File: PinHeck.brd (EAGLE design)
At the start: 359.2 x 152.3 mm, 338 parts, among them IC1 FT232RQ-REEL, IC2 PIC32MX795F512L-80I/PT, IC3 CD74HCT244E, IC4 CD74HCT244E, IC5 ULN2803A, J1 500075-1517, J11 No Load, J2 500075-1517, J3 N/A, J6 161-3507-E, P1 TC33X-2-103E, SW1 101-0134-EV, SW2 101-0134-EV, U1 P8X32A-Q44, U10 74HCT2G04GV,125, U11 74HC165D,652, U12 74HC165D,652, U14 MC74HC08ADG, U15 MC74HC08ADG, U16 MC74HC08ADG, U17 MC74HC08ADG, U18 MC74HC08ADG, U19 MC74HC08ADG, U2 FT230XS-R, U20 TIP107, U21 TIP107, U22 TIP107, U23 TIP107, U24 TIP107, U25 TIP107, U26 TIP107, U27 TIP107, U28 TIP102, U29 TIP102, U3 74HC595D-Q100, U30 TIP102, U31 TIP102, U32 TIP102, U33 TIP102, U34 TIP102, U35 TIP102, U36 WS2801, U37 TIP102, U38 WS2801, U39 LM2937IMP-3.3/NOPB, U4 CAT24M01XI-T2, U40 TIP102, U41 TIP102, U42 TIP102, U43 TIP102, U44 TIP102, U45 TIP102, U46 TIP102, U47 TIP102, U48 TIP102, U49 TIP102, U5 74HC595D-Q100, U50 TIP102, U51 TIP102, U52 CD74HC123M96, U6 TIP102, U7 TIP102, U8 TIP102, U9 TIP102, X1 FQ7050B-8.000, X2 ECS-65-20-4X

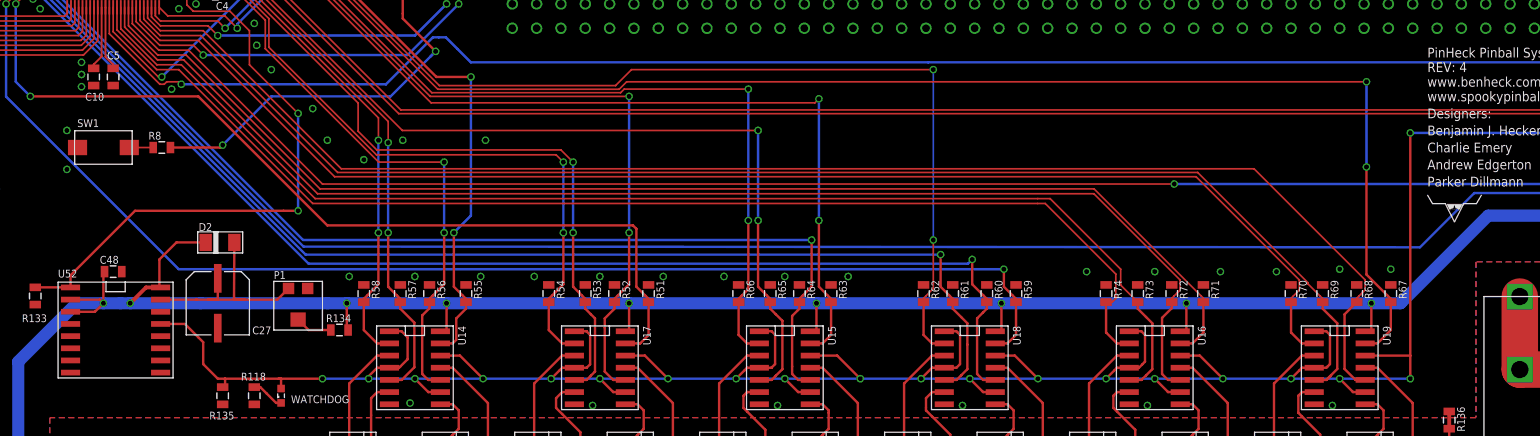
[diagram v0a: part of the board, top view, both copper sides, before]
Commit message: Rev 5 push. Fixed Bom issues and pinout for 556.
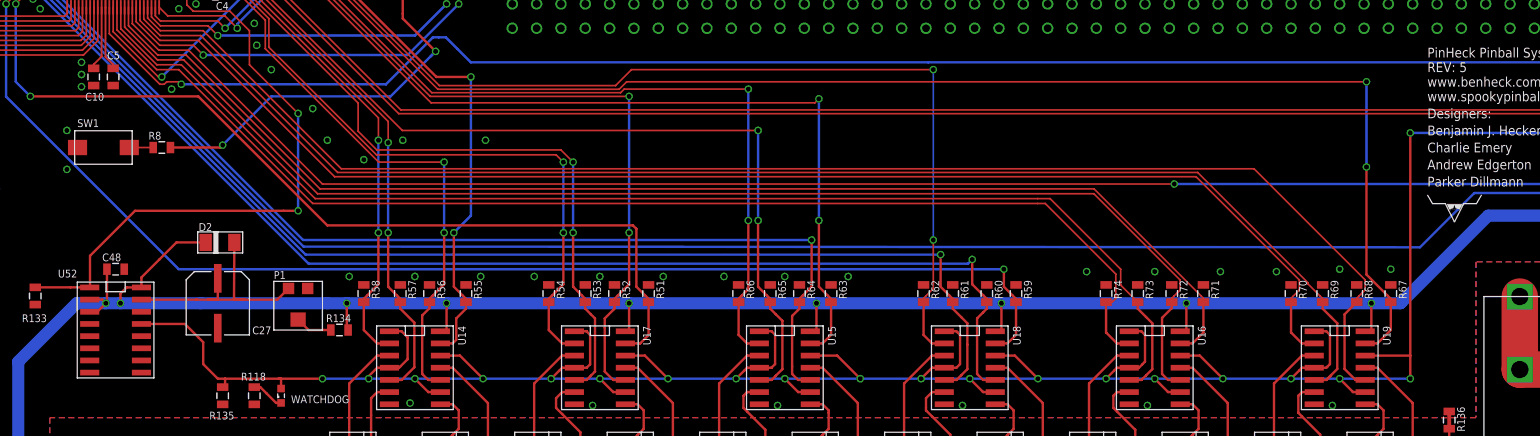
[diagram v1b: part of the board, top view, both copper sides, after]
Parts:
- IC1: value FT232RQ-REEL -> FT232RL-REEL
- U4: value CAT24M01XI-T2 -> 24LC1025-I/P
- moved C48 0.36 mm to (98.3, 86.6)
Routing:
- net 5V: track 950.2 -> 948.1 mm
- net WATCHDOG_ADJUST: track 24.1 -> 26.1 mm
- net WATCHDOG: track 343.2 -> 345.2 mm
- net PIC_ENABLE: track 62.5 -> 63.7 mm
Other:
- board text added: "REV: 5"
- board text removed: "REV: 4"
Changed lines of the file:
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@@
 <?xml version="1.0" encoding="utf-8"?>
 <!DOCTYPE eagle SYSTEM "eagle.dtd">
-<eagle version="6.5.0">
+<eagle version="6.3">
 <drawing>
 <settings>
@@
 <text x="316.992" y="110.998" size="0.8128" layer="21" font="vector">GND</text>
 <text x="235.204" y="108.712" size="1.016" layer="21">PinHeck Pinball System</text>
-<text x="235.204" y="107.188" size="1.016" layer="21">REV: 4</text>
+<text x="235.204" y="107.188" size="1.016" layer="21">REV: 5</text>
 <text x="235.204" y="102.362" size="1.016" layer="21">Designers:</text>
 <text x="235.204" y="105.664" size="1.016" layer="21">www.benheck.com</text>
@@
 </autorouter>
 <elements>
-<element name="IC1" library="IC" package="SSOP28L" value="FT232RQ-REEL" x="54.864" y="161.036" smashed="yes" rot="R90">
+<element name="IC1" library="IC" package="SSOP28L" value="FT232RL-REEL" x="54.864" y="161.036" smashed="yes" rot="R90">
 <attribute name="NAME" x="52.294" y="154.902" size="0.8128" layer="25" font="vector"/>
 </element>
@@
 <attribute name="NAME" x="275.0185" y="126.873" size="0.8128" layer="25" font="vector" rot="R90"/>
 </element>
-<element name="U4" library="PP_DigitalIC" package="DIP-8" value="CAT24M01XI-T2" x="298.704" y="150.876"/>
+<element name="U4" library="PP_DigitalIC" package="DIP-8" value="24LC1025-I/P" x="298.704" y="150.876"/>
 <element name="R16" library="PP_Passives" package="0805" value="10K" x="308.356" y="155.28925" rot="R90"/>
 <element name="R17" library="PP_Passives" package="0805" value="10K" x="305.84775" y="155.321" rot="R90"/>
@@
 </element>
 <element name="U39" library="PP_PowerIC" package="SOT-223" value="LM2937IMP-3.3/NOPB" x="32.258" y="162.56"/>
-<element name="C48" library="PP_Passives" package="0805" value="1uF" x="98.044" y="86.36"/>
+<element name="C48" library="PP_Passives" package="0805" value="1uF" x="98.298" y="86.614"/>
 <element name="C51" library="PP_Passives" package="1206" value="10uF" x="311.912" y="167.132" smashed="yes" rot="R90">
 <attribute name="NAME" x="310.896" y="163.195" size="0.8128" layer="25" font="vector"/>
@@
 <wire x1="88.138" y1="44.958" x2="88.138" y2="76.962" width="1.27" layer="16"/>
 <wire x1="88.138" y1="76.962" x2="94.234" y2="83.058" width="1.27" layer="16"/>
-<wire x1="94.234" y1="83.058" x2="97.028" y2="83.058" width="1.27" layer="16"/>
-<wire x1="97.028" y1="83.058" x2="98.806" y2="83.058" width="1.27" layer="16"/>
-<wire x1="98.806" y1="83.058" x2="99.822" y2="83.058" width="1.27" layer="16"/>
-<wire x1="99.822" y1="83.058" x2="107.188" y2="83.058" width="1.27" layer="16"/>
+<wire x1="94.234" y1="83.058" x2="97.282" y2="83.058" width="1.27" layer="16"/>
+<wire x1="97.282" y1="83.058" x2="98.806" y2="83.058" width="1.27" layer="16"/>
+<wire x1="98.806" y1="83.058" x2="107.188" y2="83.058" width="1.27" layer="16"/>
 <wire x1="107.188" y1="83.058" x2="120.396" y2="83.058" width="1.27" layer="16"/>
 <wire x1="120.396" y1="83.058" x2="122.428" y2="83.058" width="1.27" layer="16"/>
@@
 <wire x1="190.754" y1="83.058" x2="210.058" y2="83.058" width="1.27" layer="16"/>
 <wire x1="210.058" y1="83.058" x2="229.362" y2="83.058" width="1.27" layer="16"/>
-<via x="99.822" y="83.058" extent="1-16" drill="0.5"/>
+<via x="98.806" y="83.058" extent="1-16" drill="0.5"/>
 <contactref element="C48" pad="1"/>
 <wire x1="132.2" y1="80.137" x2="132.842" y2="80.137" width="0.254" layer="1"/>
@@
 <contactref element="R134" pad="2"/>
 <contactref element="D2" pad="1"/>
-<wire x1="102.998" y1="84.709" x2="101.473" y2="84.709" width="0.4064" layer="1"/>
-<wire x1="101.473" y1="84.709" x2="99.822" y2="83.058" width="0.4064" layer="1"/>
+<wire x1="100.998" y1="84.709" x2="101.473" y2="84.709" width="0.4064" layer="1"/>
 <wire x1="107.696" y1="89.408" x2="104.648" y2="89.408" width="0.254" layer="1"/>
 <wire x1="104.648" y1="89.408" x2="102.87" y2="87.63" width="0.254" layer="1"/>
-<wire x1="102.87" y1="87.63" x2="102.87" y2="84.837" width="0.254" layer="1"/>
-<wire x1="102.87" y1="84.837" x2="102.998" y2="84.709" width="0.254" layer="1"/>
-<wire x1="97.144" y1="86.36" x2="97.028" y2="86.244" width="0.254" layer="1"/>
-<wire x1="97.028" y1="86.244" x2="97.028" y2="83.058" width="0.254" layer="1"/>
-<via x="97.028" y="83.058" extent="1-16" drill="0.5"/>
-<wire x1="97.028" y1="83.058" x2="98.806" y2="83.058" width="0.254" layer="16"/>
-<wire x1="93.598" y1="83.439" x2="96.647" y2="83.439" width="0.254" layer="1"/>
-<wire x1="96.647" y1="83.439" x2="97.028" y2="83.058" width="0.254" layer="1"/>
-<wire x1="93.598" y1="82.169" x2="96.139" y2="82.169" width="0.254" layer="1"/>
-<wire x1="96.139" y1="82.169" x2="97.028" y2="83.058" width="0.254" layer="1"/>
+<via x="97.282" y="83.058" extent="1-16" drill="0.5"/>
+<wire x1="97.282" y1="83.058" x2="98.806" y2="83.058" width="0.254" layer="16"/>
+<wire x1="95.598" y1="82.169" x2="96.139" y2="82.169" width="0.254" layer="1"/>
 <wire x1="122.566" y1="80.264" x2="122.428" y2="80.402" width="0.254" layer="1"/>
 <wire x1="122.428" y1="80.402" x2="122.428" y2="83.058" width="0.254" layer="1"/>
 <via x="122.428" y="83.058" extent="1-16" drill="0.5"/>
 <wire x1="122.428" y1="83.058" x2="120.396" y2="83.058" width="0.254" layer="16"/>
+<wire x1="102.87" y1="87.63" x2="100.998" y2="85.758" width="0.254" layer="1"/>
+<wire x1="100.998" y1="85.758" x2="100.998" y2="84.709" width="0.254" layer="1"/>
+<wire x1="98.806" y1="83.058" x2="98.806" y2="84.074" width="0.254" layer="1"/>
+<wire x1="98.806" y1="84.074" x2="99.314" y2="84.582" width="0.254" layer="1"/>
+<wire x1="99.314" y1="84.582" x2="99.441" y2="84.709" width="0.254" layer="1"/>
+<wire x1="99.441" y1="84.709" x2="100.998" y2="84.709" width="0.254" layer="1"/>
+<wire x1="97.282" y1="83.058" x2="97.398" y2="83.174" width="0.254" layer="1"/>
+<wire x1="97.398" y1="83.174" x2="97.398" y2="86.614" width="0.254" layer="1"/>
+<wire x1="95.598" y1="82.169" x2="96.393" y2="82.169" width="0.254" layer="1"/>
+<wire x1="96.393" y1="82.169" x2="97.282" y2="83.058" width="0.254" layer="1"/>
+<wire x1="95.598" y1="83.439" x2="96.901" y2="83.439" width="0.254" layer="1"/>
+<wire x1="96.901" y1="83.439" x2="97.282" y2="83.058" width="0.254" layer="1"/>
 </signal>
 <signal name="DATA_LAT">
@@
 <contactref element="U52" pad="13"/>
 <contactref element="R135" pad="1"/>
-<wire x1="102.998" y1="80.899" x2="105.537" y2="80.899" width="0.254" layer="1"/>
+<wire x1="100.998" y1="80.899" x2="105.537" y2="80.899" width="0.254" layer="1"/>
 <wire x1="105.537" y1="80.899" x2="106.934" y2="79.502" width="0.254" layer="1"/>
 <wire x1="106.934" y1="79.502" x2="107.442" y2="78.994" width="0.254" layer="1"/>
@@
 <wire x1="117.348" y1="92.71" x2="115.824" y2="92.71" width="0.254" layer="1"/>
 <wire x1="115.824" y1="92.71" x2="100.33" y2="92.71" width="0.254" layer="1"/>
-<wire x1="100.33" y1="92.71" x2="93.598" y2="85.978" width="0.254" layer="1"/>
-<wire x1="93.598" y1="85.978" x2="93.598" y2="84.709" width="0.254" layer="1"/>
-<wire x1="93.598" y1="84.709" x2="93.587" y2="84.72" width="0.254" layer="1"/>
+<wire x1="100.33" y1="92.71" x2="95.63" y2="88.01" width="0.254" layer="1"/>
+<wire x1="95.598" y1="84.709" x2="93.587" y2="84.72" width="0.254" layer="1"/>
 <wire x1="93.587" y1="84.72" x2="89.916" y2="84.72" width="0.254" layer="1"/>
+<wire x1="95.63" y1="88.01" x2="95.63" y2="84.741" width="0.254" layer="1"/>
+<wire x1="95.63" y1="84.741" x2="95.598" y2="84.709" width="0.254" layer="1"/>
 </signal>
 <signal name="SOL_20">
@@
 <contactref element="P1" pad="3"/>
 <contactref element="D2" pad="2"/>
-<wire x1="106.747" y1="83.439" x2="102.998" y2="83.439" width="0.254" layer="1"/>
+<wire x1="106.747" y1="83.439" x2="100.998" y2="83.439" width="0.254" layer="1"/>
 <wire x1="116.348" y1="84.604" x2="115.183" y2="83.439" width="0.254" layer="1"/>
 <wire x1="115.183" y1="83.439" x2="111.76" y2="83.439" width="0.254" layer="1"/>
@@
 </signal>
 </signals>
-<errors>
-</errors>
 </board>
 </drawing>

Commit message: Changed some resistors to there correct number.
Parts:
- R11: value 470 -> 360
- R5: value 330 -> 360
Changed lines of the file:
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@@
 <element name="C12" library="PP_Passives" package="0805" value=".1uF" x="60.706" y="166.37" rot="R270"/>
 <element name="PIC_USB" library="PP_LED" package="LED_0402" value="VLMG1500-GS08" x="67.31" y="169.926" rot="R90"/>
-<element name="R11" library="PP_Passives" package="0805" value="470" x="67.31" y="166.37" rot="R90"/>
+<element name="R11" library="PP_Passives" package="0805" value="360" x="67.31" y="166.37" rot="R90"/>
 <element name="C2" library="PP_Passives" package="0805" value=".1uF" x="100.33" y="133.858"/>
 <element name="C3" library="PP_Passives" package="0805" value=".1uF" x="110.49" y="122.428"/>
@@
 <element name="C15" library="PP_Passives" package="0805" value=".1uF" x="265.684" y="165.608" rot="R270"/>
 <element name="C16" library="PP_Passives" package="0805" value=".1uF" x="266.7" y="159.258" rot="R90"/>
-<element name="R5" library="PP_Passives" package="0805" value="330" x="269.494" y="165.354" rot="R90"/>
+<element name="R5" library="PP_Passives" package="0805" value="360" x="269.494" y="165.354" rot="R90"/>
 <element name="PROP_RX" library="led" package="SML0603" value="VLMG1500-GS08" x="272.288" y="168.402" smashed="yes" rot="R90">
 <attribute name="NAME" x="271.288" y="167.402" size="0.8128" layer="25" font="vector" rot="R90"/>

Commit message: Changed LEDs to 0805 package.
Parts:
- removed H11: MOUNT-HOLE3.2, holes:3,2
- removed WATCHDOG: VLMG1500-GS08, led:SML0603
- added WD: LG R971-KN-1, PP_LED:LED_0805
- PIC_RX, PIC_TX, PIC_USB: value VLMG1500-GS08 -> LG R971-KN-1; device PP_LED:LED_0402 -> PP_LED:LED_0805
- PROP_ACT, PROP_RX, PROP_TX, PROP_USB, PSU_PWR: value VLMG1500-GS08 -> LG R971-KN-1; device led:SML0603 -> PP_LED:LED_0805
- moved R30 3.07 mm to (261.9, 145.3), turned to 180 degrees
- moved PROP_TX 2.96 mm to (277.6, 169.9)
- moved R15 2.54 mm to (277.6, 165.4)
- moved PROP_RX 2.16 mm to (273.8, 169.9)
- moved PROP_USB 1.55 mm to (269.7, 169.9)
- moved R6 1.52 mm to (273.8, 165.4)
- moved PIC_USB 1.14 mm to (66.3, 170.4)
- moved PSU_PWR 1.02 mm to (37.8, 162.8)
- moved R11 1.02 mm to (66.3, 166.4)
- moved PIC_TX 0.92 mm to (73.4, 170.4)
- moved PROP_ACT 0.92 mm to (261.9, 147.3)
- moved R7 0.80 mm to (73.4, 166.1)
- moved R118 0.76 mm to (112.0, 73.4), turned to 180 degrees
- moved PIC_RX 0.57 mm to (69.8, 170.4)
- moved R9 0.25 mm to (70.1, 166.1)
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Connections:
- net 3.3V: now also PSU_PWR.ANODE; no longer PSU_PWR.A
- net D1: now also PROP_USB.CATHODE; no longer PROP_USB.C
- net D2: now also PROP_RX.CATHODE; no longer PROP_RX.C
- net D3: now also PROP_TX.CATHODE; no longer PROP_TX.C
- net N$3: now also PROP_ACT.CATHODE; no longer PROP_ACT.C
- net N$50: now also WD.CATHODE; no longer WATCHDOG.C
- net N$51: now also PSU_PWR.CATHODE; no longer PSU_PWR.C
- net P27: now also PROP_ACT.ANODE; no longer PROP_ACT.A
- net VBUS_PROP: now also PROP_RX.ANODE, PROP_TX.ANODE, PROP_USB.ANODE; no longer PROP_RX.A, PROP_TX.A, PROP_USB.A
- net WATCHDOG: now also WD.ANODE; no longer WATCHDOG.A
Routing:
- net VBUS_PROP: track 28.4 -> 32.5 mm
- net FT_3.3V: track 46.0 -> 47.9 mm
- net TXLED: track 25.1 -> 26.9 mm
- net D3: track 1.40 -> 2.62 mm
- net D2: track 1.40 -> 2.62 mm
- net D1: track 1.40 -> 2.62 mm
- net WATCHDOG: track 345.2 -> 346.0 mm
- net N$498: track 1.78 -> 2.54 mm
- net N$51: track 1.65 -> 2.37 mm
- net RXLED: track 10.6 -> 11.3 mm
- net N$50: track 3.48 -> 2.88 mm
- net N$11: track 38.9 -> 39.5 mm
- net P27: track 8.83 -> 9.35 mm
- net GND: vias 104 -> 106
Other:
- board text added: "REV: 6"
- board text removed: "REV: 5"
